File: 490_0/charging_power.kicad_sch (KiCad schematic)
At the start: 63 parts, among them J18 B3B-XH-A, J19 S2B-XH-A, J22 2171790001, SW1 SW_Push, SW10 SW_Push, SW11 SW_Push, U4 MP2639AGR-Z, U8 MP2632BGR-Z

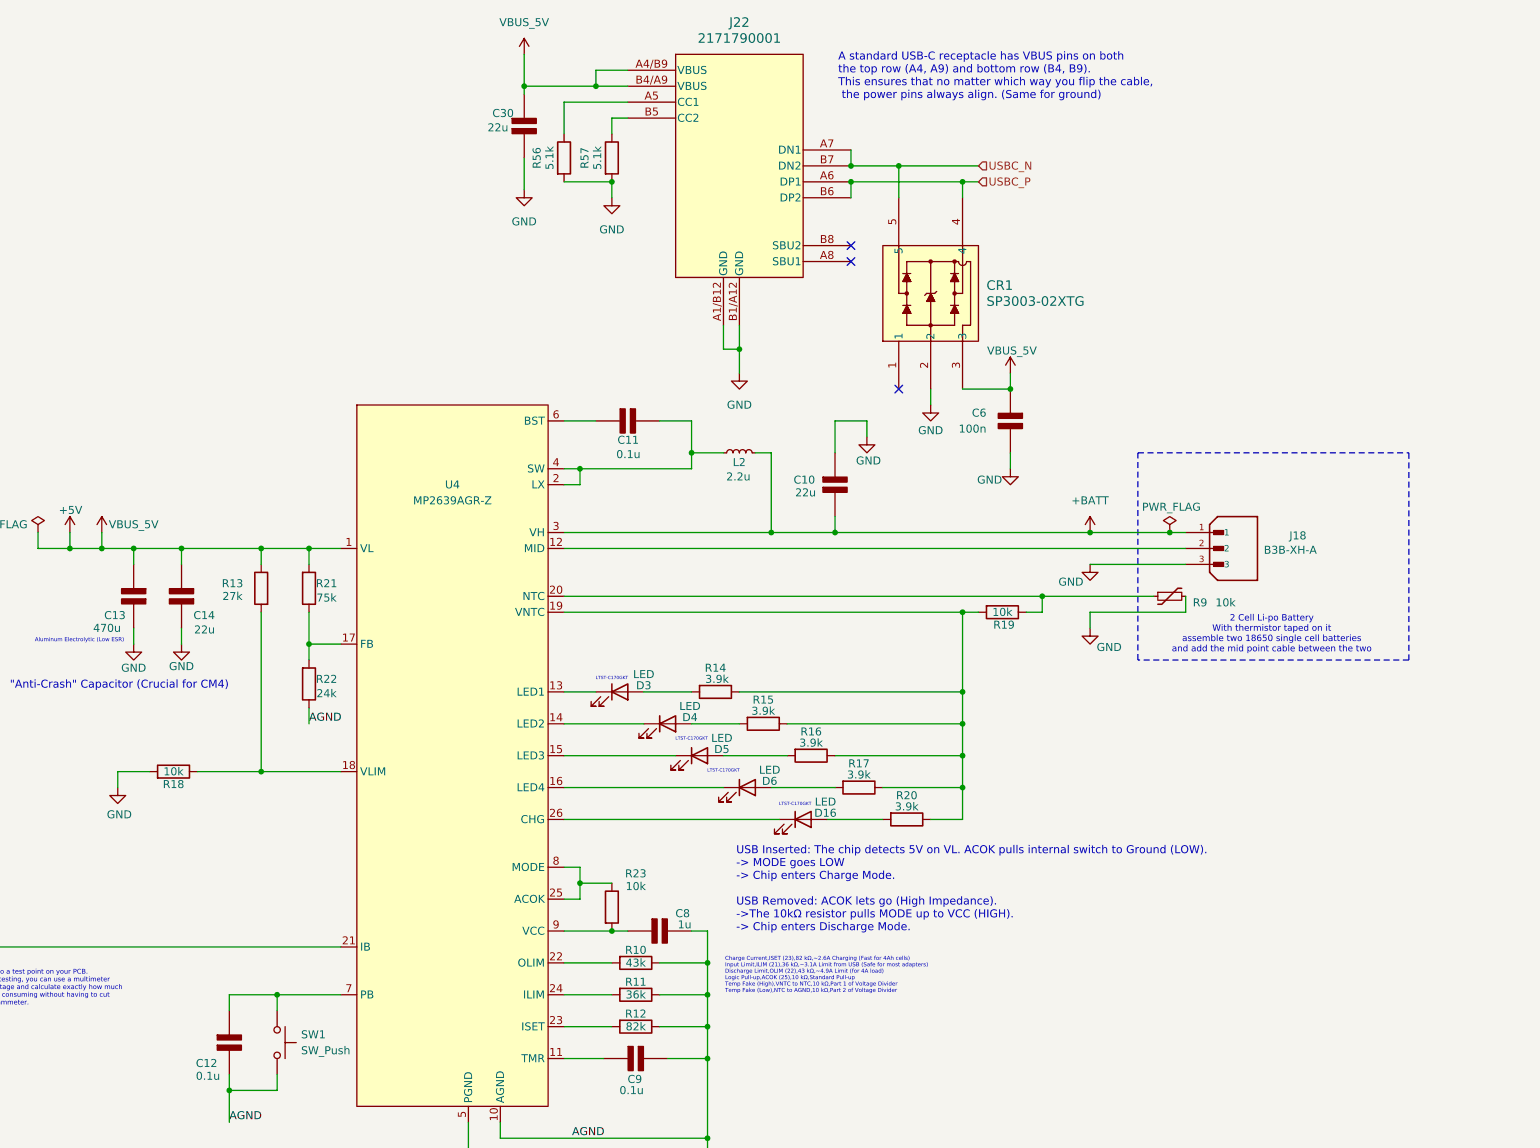
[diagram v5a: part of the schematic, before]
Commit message: Finished power circuit
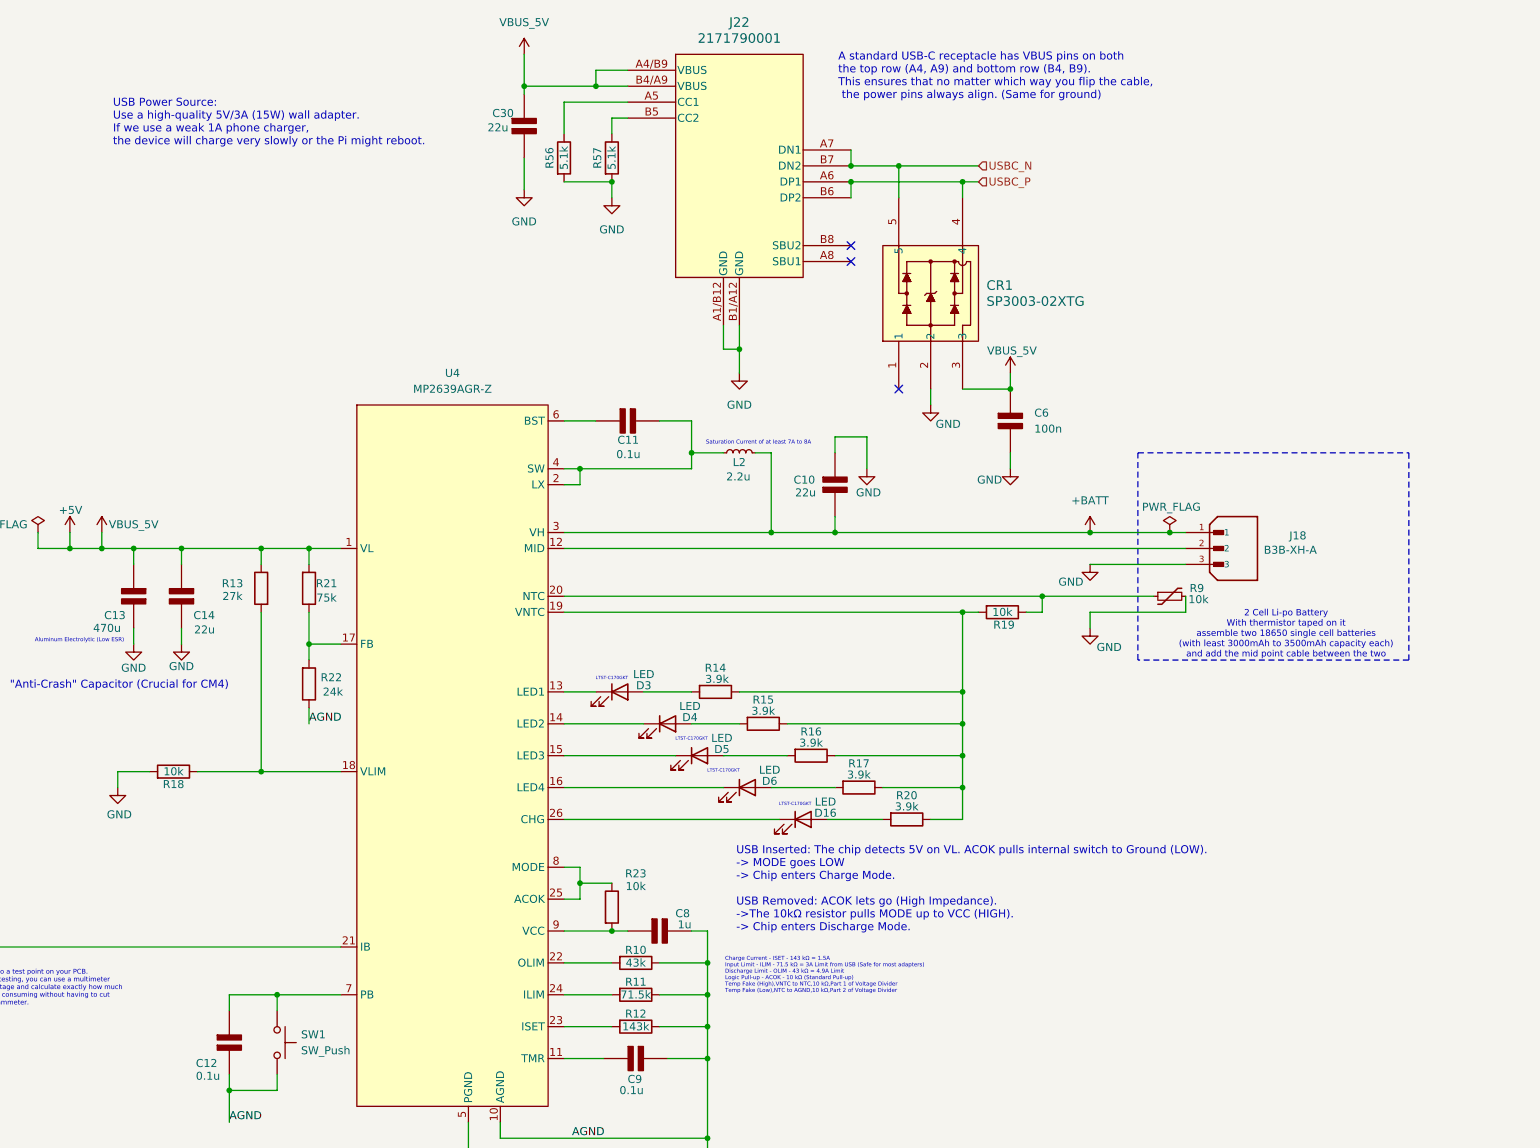
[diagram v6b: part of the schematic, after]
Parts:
- R11: value 36k -> 71.5k
- R12: value 82k -> 143k
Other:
- note added: "2 Cell Li-po Battery With thermistor taped on it assemble two 18650 single cell batteries (with least 3000mAh to 3500mAh capacity each) and add the mid point cable between the two"
- note added: "Charge Current - ISET - 143 kΩ = 1.5A Input Limit - ILIM - 71.5 kΩ = 3A Limit from USB (Safe for most adapters) Discharge Limit - OLIM - 43 kΩ = 4.9A Limit Logic Pull-up - ACOK - 10 kΩ (Standard Pull-up) Temp Fake (High),VNTC to NTC,10 kΩ,Part 1 of Voltage Divider Temp Fake (Low),NTC to AGND,10 kΩ,Part 2 of Voltage Divider"
- note added: "Saturation Current of at least 7A to 8A"
- note added: "USB Power Source: Use a high-quality 5V/3A (15W) wall adapter. If we use a weak 1A phone charger, the device will charge very slowly or the Pi might reboot."
- note removed: "2 Cell Li-po Battery With thermistor taped on it assemble two 18650 single cell batteries and add the mid point cable between the two"
- note removed: "Charge Current,ISET (23),82 kΩ,~2.6A Charging (Fast for 4Ah cells) Input Limit,ILIM (21),36 kΩ,~3.1A Limit from USB (Safe for most adapters) Discharge Limit,OLIM (22),43 kΩ,~4.9A Limit (for 4A load) Logic Pull-up,ACOK (25),10 kΩ,Standard Pull-up Temp Fake (High),VNTC to NTC,10 kΩ,Part 1 of Voltage Divider Temp Fake (Low),NTC to AGND,10 kΩ,Part 2 of Voltage Divider"

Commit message: Power + BOM update
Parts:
- removed C13: 470u, symbol PCM_Elektuur:C
- removed C29, C30, C31, C32: 22u, symbol PCM_Elektuur:C
- removed C34: 0.1u, symbol PCM_Elektuur:C
- removed C6: 100n, symbol PCM_Elektuur:C
- removed CR1: SP3003-02XTG, SOT553_LTF, symbol capstone_parts:SP3003-02XTG
- removed D17, D18, D19, D20: LED, symbol Device:LED
- removed J19: S2B-XH-A, S2B-XH-A:JST_S2B-XH-A, symbol capstone_parts:S2B-XH-A
- removed J22: 2171790001, 2171790001_MOL, symbol capstone_parts:2171790001
- removed JP8: SolderJumper_3_Open, symbol Jumper:SolderJumper_3_Open
- removed R23, R52: 10k, symbol Device:R
- removed R51: 10m, symbol Device:R
- removed R55: 10k, symbol PCM_SparkFun-Resistor:Thermistor-NTC-10k
- removed R56, R57: 5.1k, symbol Device:R
- removed R58, R59, R60, R61: 3.9k, symbol Device:R
- removed R62: 49.9k, symbol Device:R
- removed R63: 13k, symbol Device:R
- removed SW10, SW11: SW_Push, symbol Switch:SW_Push
- removed U8: MP2632BGR-Z, IC26_MP2632BGR-Z_MNP, symbol capstone_parts:MP2632BGR-Z
- added C37: 47u, symbol PCM_Elektuur:C
- added C38, C42: open, symbol PCM_Elektuur:C
- added C39, C40: 4.7u, symbol PCM_Elektuur:C
- added C41, C43: 0.01u, symbol PCM_Elektuur:C
- added C44: 2200p, symbol PCM_Elektuur:C
- added C45: 22p, symbol PCM_Elektuur:C
- added C49: 22u, symbol PCM_Elektuur:C
- added D10: SMF5.0A, symbol PCM_Diode_TVS_AKL:SMF5.0A
- added NT1: NetTie_2, symbol Device:NetTie_2
- added R37: 51.1, symbol Device:R
- added R38: 200k, symbol Device:R
- added R39: 10.2k, symbol Device:R
- added R40: 47k, symbol Device:R
- added R41: 1.96k, symbol Device:R
- added R42: 37.4k, symbol Device:R
- added U7: TPS54531DDA, symbol capstone_parts:TPS54531DDA
- C35: now fitted; now in the parts list
- C36: value 0.1u -> 47u; now fitted; now in the parts list
- D11: renamed from D3; Digikey Link (none) -> https://www.digikey.ca/en/products/detail/liteon/LTST-C170G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; Manufacturer (none) -> Lite-On Inc.; Manufacturer Part (none) -> LTST-C170GKT; Package (none) -> SMD; Price (none) -> 0.10; Supplier (none) -> DigiKey; Supplier P/N (none) -> 160-1179-1-ND; Type (none) -> 0805 (2012 Metric); Unit (none) -> pcs
- D12: renamed from D4; Digikey Link (none) -> https://www.digikey.ca/en/products/detail/liteon/LTST-C170G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; Manufacturer (none) -> Lite-On Inc.; Manufacturer Part (none) -> LTST-C170GKT; Package (none) -> SMD; Price (none) -> 0.10; Supplier (none) -> DigiKey; Supplier P/N (none) -> 160-1179-1-ND; Type (none) -> 0805 (2012 Metric); Unit (none) -> pcs
- D13: renamed from D5; Digikey Link (none) -> https://www.digikey.ca/en/products/detail/liteon/LTST-C170G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; Manufacturer (none) -> Lite-On Inc.; Manufacturer Part (none) -> LTST-C170GKT; Package (none) -> SMD; Price (none) -> 0.10; Supplier (none) -> DigiKey; Supplier P/N (none) -> 160-1179-1-ND; Type (none) -> 0805 (2012 Metric); Unit (none) -> pcs
- D14: renamed from D6; Digikey Link (none) -> https://www.digikey.ca/en/products/detail/liteon/LTST-C170G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; Manufacturer (none) -> Lite-On Inc.; Manufacturer Part (none) -> LTST-C170GKT; Package (none) -> SMD; Price (none) -> 0.10; Supplier (none) -> DigiKey; Supplier P/N (none) -> 160-1179-1-ND; Type (none) -> 0805 (2012 Metric); Unit (none) -> pcs
- D16: Digikey Link (none) -> https://www.digikey.ca/en/products/detail/lite-on-inc/LTST-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; Manufacturer (none) -> Lite-On Inc.; Manufacturer Part (none) -> LTST-C170YKT; Package (none) -> SMD; Price (none) -> 0.15; Supplier (none) -> DigiKey; Supplier P/N (none) -> 160-1175-1-ND; Type (none) -> 0805 (2012 Metric); Unit (none) -> pcs
- L1: value 2.2uH -> 4.7u; Current 1.2A -> ? A; now fitted; now in the parts list
- R43: renamed from R13; Digikey Link (none) -> https://www.digikey.ca/en/products/detail/yageo/RC1206FR-07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; Manufacturer (none) -> YAGEO; Manufacturer Part (none) -> RC1206FR-0727KL; Package (none) -> 1206; Price (none) -> 0.1; Supplier (none) -> DigiKey; Supplier P/N (none) -> 311-27.0KFRCT-ND; Type (none) -> SMD; Unit (none) -> pcs
- R44: renamed from R21; Digikey Link (none) -> https://www.digikey.ca/en/products/detail/yageo/RC1206FR-07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; Manufacturer (none) -> YAGEO; Manufacturer Part (none) -> RC1206FR-0775KL; Package (none) -> 1206; Price (none) -> 0.1; Supplier (none) -> DigiKey; Supplier P/N (none) -> 311-75.0KFRCT-ND; Type (none) -> SMD; Unit (none) -> pcs
- R48: renamed from R22; Digikey Link (none) -> https://www.digikey.ca/en/products/detail/yageo/RC1206FR-07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; Manufacturer (none) -> YAGEO; Manufacturer Part (none) -> RC1206FR-0724KL; Package (none) -> 1206; Price (none) -> 0.1; Supplier (none) -> DigiKey; Supplier P/N (none) -> 311-24.0KFRCT-ND; Type (none) -> SMD; Unit (none) -> pcs
- R49: renamed from R14; value 3.9k -> 1.5k; Digikey Link (none) -> https://www.digikey.ca/en/products/detail/yageo/RC1206FR-07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; Manufacturer (none) -> YAGEO; Manufacturer Part (none) -> RC1206FR-071K5L; Package (none) -> 1206; Price (none) -> 0.1; Supplier (none) -> DigiKey; Supplier P/N (none) -> 311-1.50KFRCT-ND; Type (none) -> SMD; Unit (none) -> pcs
- R50: renamed from R15; value 3.9k -> 1.5k; Digikey Link (none) -> https://www.digikey.ca/en/products/detail/yageo/RC1206FR-07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; Manufacturer (none) -> YAGEO; Manufacturer Part (none) -> RC1206FR-071K5L; Package (none) -> 1206; Price (none) -> 0.1; Supplier (none) -> DigiKey; Supplier P/N (none) -> 311-1.50KFRCT-ND; Type (none) -> SMD; Unit (none) -> pcs
- R53: renamed from R16; value 3.9k -> 1.5k; Digikey Link (none) -> https://www.digikey.ca/en/products/detail/yageo/RC1206FR-07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; Manufacturer (none) -> YAGEO; Manufacturer Part (none) -> RC1206FR-071K5L; Package (none) -> 1206; Price (none) -> 0.1; Supplier (none) -> DigiKey; Supplier P/N (none) -> 311-1.50KFRCT-ND; Type (none) -> SMD; Unit (none) -> pcs
- R55: renamed from R17; value 3.9k -> 1.5k; Digikey Link (none) -> https://www.digikey.ca/en/products/detail/yageo/RC1206FR-07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; Manufacturer (none) -> YAGEO; Manufacturer Part (none) -> RC1206FR-071K5L; Package (none) -> 1206; Price (none) -> 0.1; Supplier (none) -> DigiKey; Supplier P/N (none) -> 311-1.50KFRCT-ND; Type (none) -> SMD; Unit (none) -> pcs
- R57: renamed from R20; value 3.9k -> 1.5k; Digikey Link (none) -> https://www.digikey.ca/en/products/detail/yageo/RC1206FR-07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; Manufacturer (none) -> YAGEO; Manufacturer Part (none) -> RC1206FR-071K5L; Package (none) -> 1206; Price (none) -> 0.1; Supplier (none) -> DigiKey; Supplier P/N (none) -> 311-1.50KFRCT-ND; Type (none) -> SMD; Unit (none) -> pcs
- R61: renamed from R10; Digikey Link (none) -> https://www.digikey.ca/en/products/detail/yageo/RC1206FR-07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; Manufacturer (none) -> YAGEO; Manufacturer Part (none) -> RC1206FR-0743KL; Package (none) -> 1206; Price (none) -> 0.1; Supplier (none) -> DigiKey; Supplier P/N (none) -> 311-43.0KFRCT-ND; Type (none) -> SMD; Unit (none) -> pcs
- R62: renamed from R11; Digikey Link (none) -> https://www.digikey.ca/en/products/detail/yageo/RC0805FR-07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; Manufacturer (none) -> YAGEO; Manufacturer Part (none) -> RC0805FR-0771K5L; Package (none) -> 0805; Price (none) -> 0.1; Supplier (none) -> DigiKey; Supplier P/N (none) -> 311-71.5KCRCT-ND; Type (none) -> SMD; Unit (none) -> pcs
- R65: renamed from R12; value 143k -> 215k; Digikey Link (none) -> https://www.digikey.ca/en/products/detail/yageo/RC0805FR-07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; Manufacturer (none) -> YAGEO; Manufacturer Part (none) -> RC0805FR-07215KL; Package (none) -> 0805; Price (none) -> 0.1; Supplier (none) -> DigiKey; Supplier P/N (none) -> 311-215KCRCT-ND; Type (none) -> SMD; Unit (none) -> pcs
- SW9: renamed from SW1; value SW_Push -> B3F-1000; Digikey Link (none) -> https://www.digikey.ca/en/products/detail/omron-electronics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; Manufacturer (none) -> Omron Electronics Inc-EMC Div; Manufacturer Part (none) -> B3F-1000; Price (none) -> 0.24; Supplier (none) -> DigiKey; Supplier P/N (none) -> SW400-ND; Type (none) -> Through Hole; Unit (none) -> pcs
- TP1: now left out of the parts list
- U8: renamed from U4; Current - Supply (none) -> 5A; Digikey Link (none) -> https://www.digikey.ca/en/products/detail/monolithic-power-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; Manufacturer (none) -> Monolithic Power Systems Inc.; Manufacturer Part (none) -> MP2639AGR-Z; Package (none) -> 26-PowerVFQFN; Price (none) -> 3.49; Supplier (none) -> DigiKey; Supplier P/N (none) -> 1589-1618-1-ND; Type (none) -> SMD; Unit (none) -> pcs; Voltage - Supply (none) -> 5.75V
- renumbered C11 to C46, C10 to C47, C14 to C50, C8 to C54, C12 to C57, C9 to C58, J18 to J19, R9 to R45, R19 to R46, R18 to R54
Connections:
- net +5V: now also C36.2 (-), L1.2, C37.2 (-), C38.2 (-), R37.2; no longer C50.1 (+), R43.1, R44.2, U8.1 (VL)
- net GND: now also C36.1 (+), U8.8 (MODE), C37.1 (+), C38.1 (+), C39.1 (+), C40.1 (+), C41.1 (+), C43.1 (+), C45.1 (+), C49.2 (-), D10.2 (A), NT1.2, R40.1, R41.1, R42.1, U7.7 (GND), U7.EPAD; no longer C35.2 (-), C36.2 (-), C57.2 (-), R48.1, SW9.2, U8.10 (AGND)
- net at C35.1 (+): now also U7.1 (BOOT)
- net at L1.1: now also C35.2 (-), D10.1 (K), U7.8 (PH)
- net at C46.2 (-), L2.1, U8.4 (SW): no longer U8.2 (LX)
- net at U8.25 (ACOK): no longer U8.8 (MODE)
- net +BATT renamed +VBATT_8V4
- net +VBATT_8V4: now also C39.2 (-), C40.2 (-), C41.2 (-), R38.2, U7.2 (VIN); no longer L2.2
- new net: C42.1 (+), R39.1, R41.2, U7.5 (VSENSE)
- new net: C42.2 (-), R37.1, R39.2
- new net: C44.1 (+), R42.2
- new net: C44.2 (-), C45.2 (-), U7.6 (COMP)
- new net: L2.2, U8.2 (LX)
- new net: R38.1, R40.2, U7.3 (EN)
- new net: C43.2 (-), U7.4 (SS)
- new net AGND: C57.2 (-), NT1.1, R48.1, SW9.2, U8.10 (AGND)
- new net VBUS_5V: C49.1 (+), C50.1 (+), R43.1, R44.2, U8.1 (VL)
- no-connect marks 9 -> 1
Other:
- note added: "Charge Current - ISET - 215 kΩ = 1A Input Limit - ILIM - 71.5 kΩ = 3A Limit from USB (Safe for most adapters) Discharge Limit - OLIM - 43 kΩ = 4.9A Limit Logic Pull-up - ACOK - 10 kΩ (Standard Pull-up) Temp Fake (High),VNTC to NTC,10 kΩ,Part 1 of Voltage Divider Temp Fake (Low),NTC to AGND,10 kΩ,Part 2 of Voltage Divider"
- note added: "The chip doesnt need to enter discharge mode"
- note added: "rated for 16V or 25V"
- note removed: ""Anti-Crash" Capacitor (Crucial for CM4)"
- note removed: "A standard USB-C receptacle has VBUS pins on both the top row (A4, A9) and bottom row (B4, B9). This ensures that no matter which way you flip the cable, the power pins always align. (Same for ground)"
- note removed: "Aluminum Electrolytic (Low ESR)"
- note removed: "Charge Current - ISET - 143 kΩ = 1.5A Input Limit - ILIM - 71.5 kΩ = 3A Limit from USB (Safe for most adapters) Discharge Limit - OLIM - 43 kΩ = 4.9A Limit Logic Pull-up - ACOK - 10 kΩ (Standard Pull-up) Temp Fake (High),VNTC to NTC,10 kΩ,Part 1 of Voltage Divider Temp Fake (Low),NTC to AGND,10 kΩ,Part 2 of Voltage Divider"
- note removed: "LTST-C170GKT"
- note removed: "Single Cell Li-po Battery"
- note removed: "Tape the NTC thermistor to the battery cell with thermal tape"
- note removed: "USB Inserted: The chip detects 5V on VL. ACOK pulls internal switch to Ground (LOW). -> MODE goes LOW -> Chip enters Charge Mode. USB Removed: ACOK lets go (High Impedance). ->The 10kΩ resistor pulls MODE up to VCC (HIGH). -> Chip enters Discharge Mode."
- note removed: "USB Power Source: Use a high-quality 5V/3A (15W) wall adapter. If we use a weak 1A phone charger, the device will charge very slowly or the Pi might reboot."
- note removed: "VBATT"
- note removed: "^For Charge current"

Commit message: finished BOM
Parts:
- C35, C46, C57, C58: Digikey Link (none) -> https://www.digikey.ca/en/products/detail/samsung-electro-m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; Manufacturer (none) -> Samsung Electro-Mechanics; Manufacturer Part (none) -> CL31B104KBCNNNC; Package (none) -> 1206 (3216 Metric); Price (none) -> 0.11; Supplier (none) -> DigiKey; Supplier P/N (none) -> 1276-1017-1-ND; Type (none) -> SMD, MLCC; Unit (none) -> pcs
- C36, C37: Digikey Link (none) -> https://www.digikey.ca/en/products/detail/samsung-electro-m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; Manufacturer (none) -> Samsung Electro-Mechanics; Manufacturer Part (none) -> CL31A476MQHNNNE; Package (none) -> 1206 (3216 Metric); Price (none) -> 0.31; Supplier (none) -> DigiKey; Supplier P/N (none) -> 1276-1167-1-ND; Type (none) -> SMD, MLCC; Unit (none) -> pcs
- C39, C40: Digikey Link (none) -> https://www.digikey.ca/en/products/detail/kemet/c1206c475k3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; Manufacturer (none) -> KEMET; Manufacturer Part (none) -> C1206C475K3RACTU; Package (none) -> 1206 (3216 Metric); Price (none) -> 0.52; Supplier (none) -> DigiKey; Supplier P/N (none) -> 399-C1206C475K3RACTUCT-ND; Type (none) -> SMD; Unit (none) -> pcs
- C41, C43: Digikey Link (none) -> https://www.digikey.ca/en/products/detail/kemet/c1206c103k5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; Manufacturer (none) -> KEMET; Manufacturer Part (none) -> C1206C103K5RACTU; Package (none) -> 1206 (3216 Metric); Price (none) -> 0.15; Supplier (none) -> DigiKey; Supplier P/N (none) -> 399-C1206C103K5RACTUCT-ND; Type (none) -> SMD; Unit (none) -> pcs
- C44: Digikey Link (none) -> https://www.digikey.ca/en/products/detail/kemet/c1206c222k5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; Manufacturer (none) -> KEMET; Manufacturer Part (none) -> C1206C222K5RACTU; Package (none) -> 1206 (3216 Metric); Price (none) -> 0.19; Supplier (none) -> DigiKey; Supplier P/N (none) -> 399-C1206C222K5RACTUCT-ND; Type (none) -> SMD; Unit (none) -> pcs
- C45: Digikey Link (none) -> https://www.digikey.ca/en/products/detail/samsung-electro-m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; Manufacturer (none) -> Samsung Electro-Mechanics; Manufacturer Part (none) -> CL31C220JBCNNNC; Package (none) -> 1206 (3216 Metric); Price (none) -> 0.12; Supplier (none) -> DigiKey; Supplier P/N (none) -> 1276-1203-1-ND; Type (none) -> SMD; Unit (none) -> pcs
- C47: Digikey Link (none) -> https://www.digikey.ca/en/products/detail/samsung-electro-m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; Manufacturer (none) -> Samsung Electro-Mechanics; Manufacturer Part (none) -> CL31A226KAHNNNE; Package (none) -> 1206 (3216 Metric); Price (none) -> 0.08; Supplier (none) -> DigiKey; Supplier P/N (none) -> 1276-3047-1-ND; Type (none) -> SMD; Unit (none) -> pcs
- C49, C50: Digikey Link (none) -> https://www.digikey.ca/en/products/detail/samsung-electro-m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; Manufacturer (none) -> Samsung Electro-Mechanics; Manufacturer Part (none) -> CL31B226KPHNNNE; Package (none) -> 1206 (3216 Metric); Price (none) -> 0.39; Supplier (none) -> DigiKey; Supplier P/N (none) -> 1276-2769-1-ND; Type (none) -> SMD; Unit (none) -> pcs
- C54: Digikey Link (none) -> https://www.digikey.ca/en/products/detail/kemet/c1206c105k4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; Manufacturer (none) -> KEMET; Manufacturer Part (none) -> C1206C105K4RAC7210; Package (none) -> 1206 (3216 Metric); Price (none) -> 0.23; Supplier (none) -> DigiKey; Supplier P/N (none) -> 399-C1206C105K4RAC7210CT-ND; Type (none) -> SMD, MLCC; Unit (none) -> pcs
- J19: Digikey Link (none) -> https://www.digikey.ca/en/products/detail/jst-sales-america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; Manufacturer (none) -> JST Sales America Inc.; Manufacturer Part (none) -> B3B-XH-A; Price (none) -> 0.11; Supplier (none) -> DigiKey; Supplier P/N (none) -> 455-2248-ND; Type (none) -> Through Hole; Unit (none) -> pcs
- L1: footprint PCM_SparkFun-Coil:0806 -> (none); Digikey Link (none) -> https://www.digikey.ca/en/products/detail/bourns-inc/SRP654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; Manufacturer (none) -> Bourns Inc.; Manufacturer Part (none) -> SRP6540-4R7M; Package (none) -> Nonstandard; Price (none) -> 1.11; Supplier (none) -> DigiKey; Supplier P/N (none) -> SRP6540-4R7MCT-ND; Type (none) -> SMD; Unit (none) -> pcs
- L2: footprint PCM_SparkFun-Coil:0806 -> (none); Digikey Link (none) -> https://www.digikey.ca/en/products/detail/bourns-inc/srp654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; Manufacturer (none) -> Bourns Inc.; Manufacturer Part (none) -> SRP6540-2R2M; Package (none) -> Nonstandard; Price (none) -> 1.11; Supplier (none) -> DigiKey; Supplier P/N (none) -> SRP6540-2R2MCT-ND; Type (none) -> SMD; Unit (none) -> pcs
- R37: Digikey Link (none) -> https://www.digikey.ca/en/products/detail/yageo/RC1206FR-13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; Manufacturer (none) -> YAGEO; Manufacturer Part (none) -> RC1206FR-1351R1L; Package (none) -> 1206; Price (none) -> 0.1; Supplier (none) -> DigiKey; Supplier P/N (none) -> 13-RC1206FR-1351R1LCT-ND; Type (none) -> SMD; Unit (none) -> pcs
- R38: Digikey Link (none) -> https://www.digikey.ca/en/products/detail/yageo/RC1206FR-07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; Manufacturer (none) -> YAGEO; Manufacturer Part (none) -> RC1206FR-07200KL; Package (none) -> 1206; Price (none) -> 0.1; Supplier (none) -> DigiKey; Supplier P/N (none) -> 311-200KFRCT-ND; Type (none) -> SMD; Unit (none) -> pcs
- R39: Digikey Link (none) -> https://www.digikey.ca/en/products/detail/yageo/RC1206FR-07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; Manufacturer (none) -> YAGEO; Manufacturer Part (none) -> RC1206FR-0710K2L; Package (none) -> 1206; Price (none) -> 0.1; Supplier (none) -> DigiKey; Supplier P/N (none) -> 311-10.2KFRCT-ND; Type (none) -> SMD; Unit (none) -> pcs
- R45: Digikey Link (none) -> https://www.digikey.ca/en/products/detail/vishay-beyschlag-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; Manufacturer (none) -> Vishay Beyschlag/Draloric/BC Components; Manufacturer Part (none) -> NTCLE100E3103JB0; Price (none) -> 0.57; Supplier (none) -> DigiKey; Supplier P/N (none) -> BC2301-ND; Type (none) -> Through Hole; Unit (none) -> pcs
- R46, R54: Digikey Link (none) -> https://www.digikey.ca/en/products/detail/yageo/RC1206FR-07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; Manufacturer (none) -> YAGEO; Manufacturer Part (none) -> RC1206FR-0710KL; Package (none) -> 1206; Price (none) -> 0.1; Supplier (none) -> DigiKey; Supplier P/N (none) -> 311-10.0KFRCT-ND; Type (none) -> SMD; Unit (none) -> pcs
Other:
- note added: "2 Cell Li-po Battery With thermistor taped on it (Kapton tape) assemble two 18650 single cell batteries (with least 3000mAh to 3500mAh capacity each) and add the mid point cable between the two"
- note removed: "2 Cell Li-po Battery With thermistor taped on it assemble two 18650 single cell batteries (with least 3000mAh to 3500mAh capacity each) and add the mid point cable between the two"
